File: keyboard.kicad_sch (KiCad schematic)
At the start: 35 parts, among them J1 USB_C_Receptacle_USB2.0, J2 USB_C_Receptacle_USB2.0, SW1 SW_Push, SW10 SW_Push, SW11 SW_Push, SW12 SW_Push, SW2 SW_Push, SW3 SW_Push, SW4 SW_Push, SW5 SW_Push, SW6 SW_Push, SW7 SW_Push, SW8 SW_Push, SW9 SW_Push, U1 PCA9555PW, U2 PCA9555PW, U3 SeeeduinoXIAO

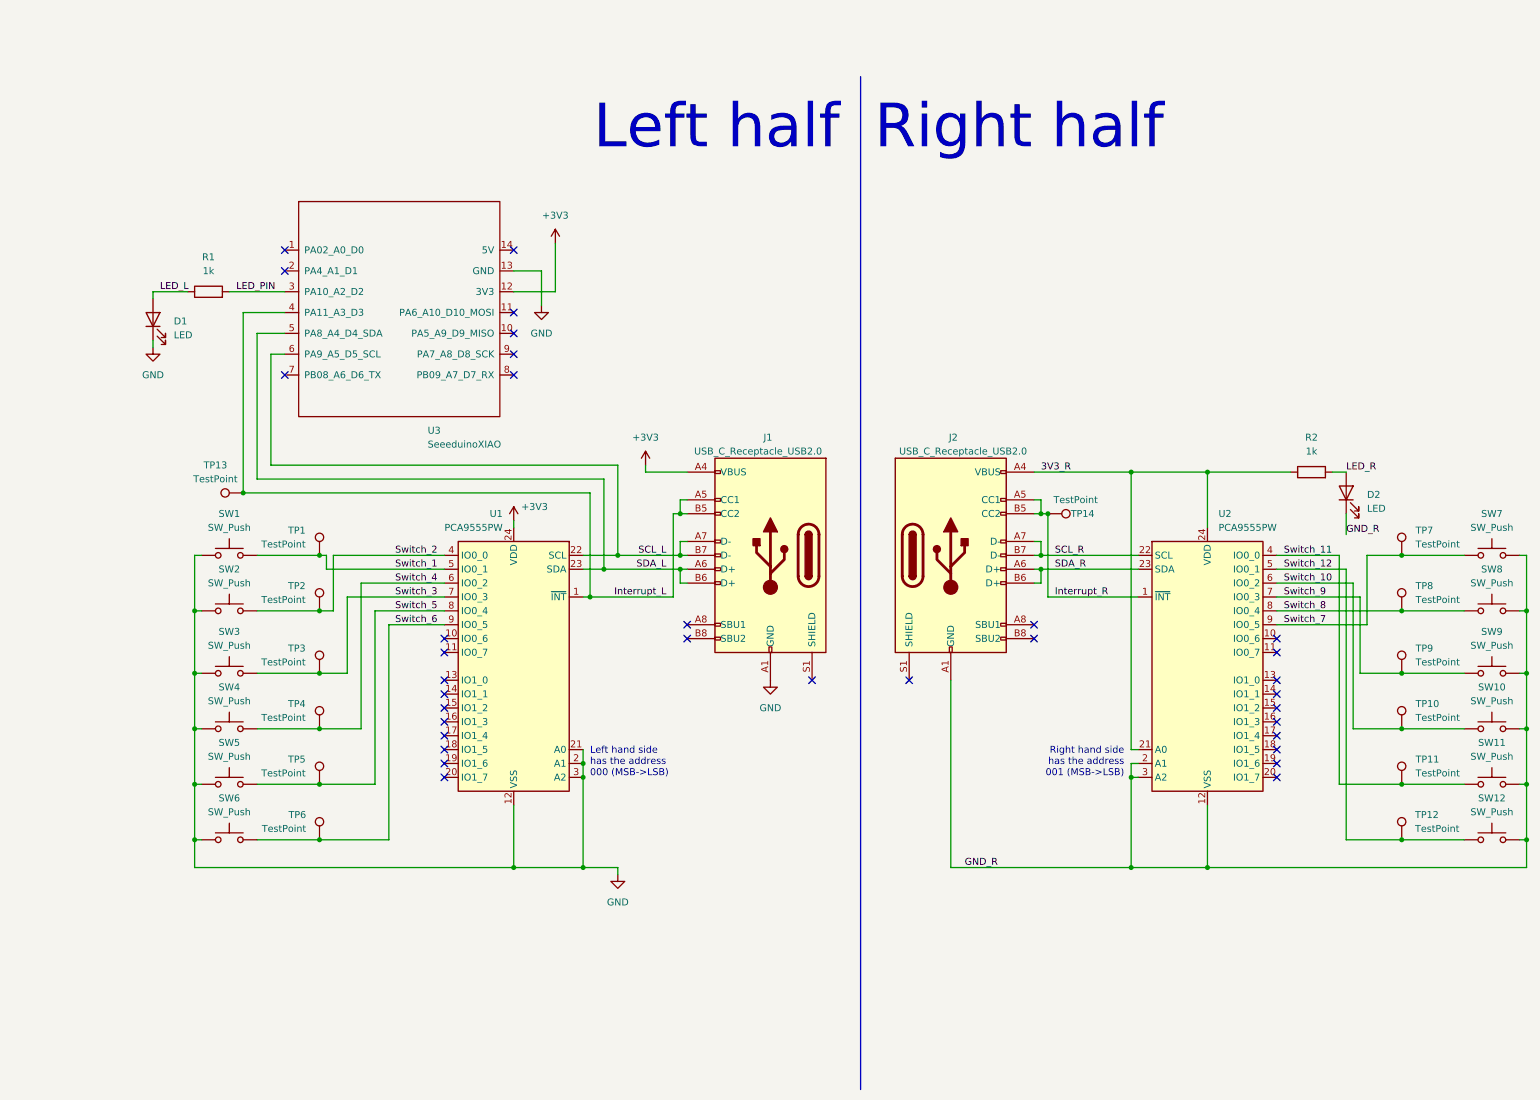
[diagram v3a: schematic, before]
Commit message: Went back to TRRS connection
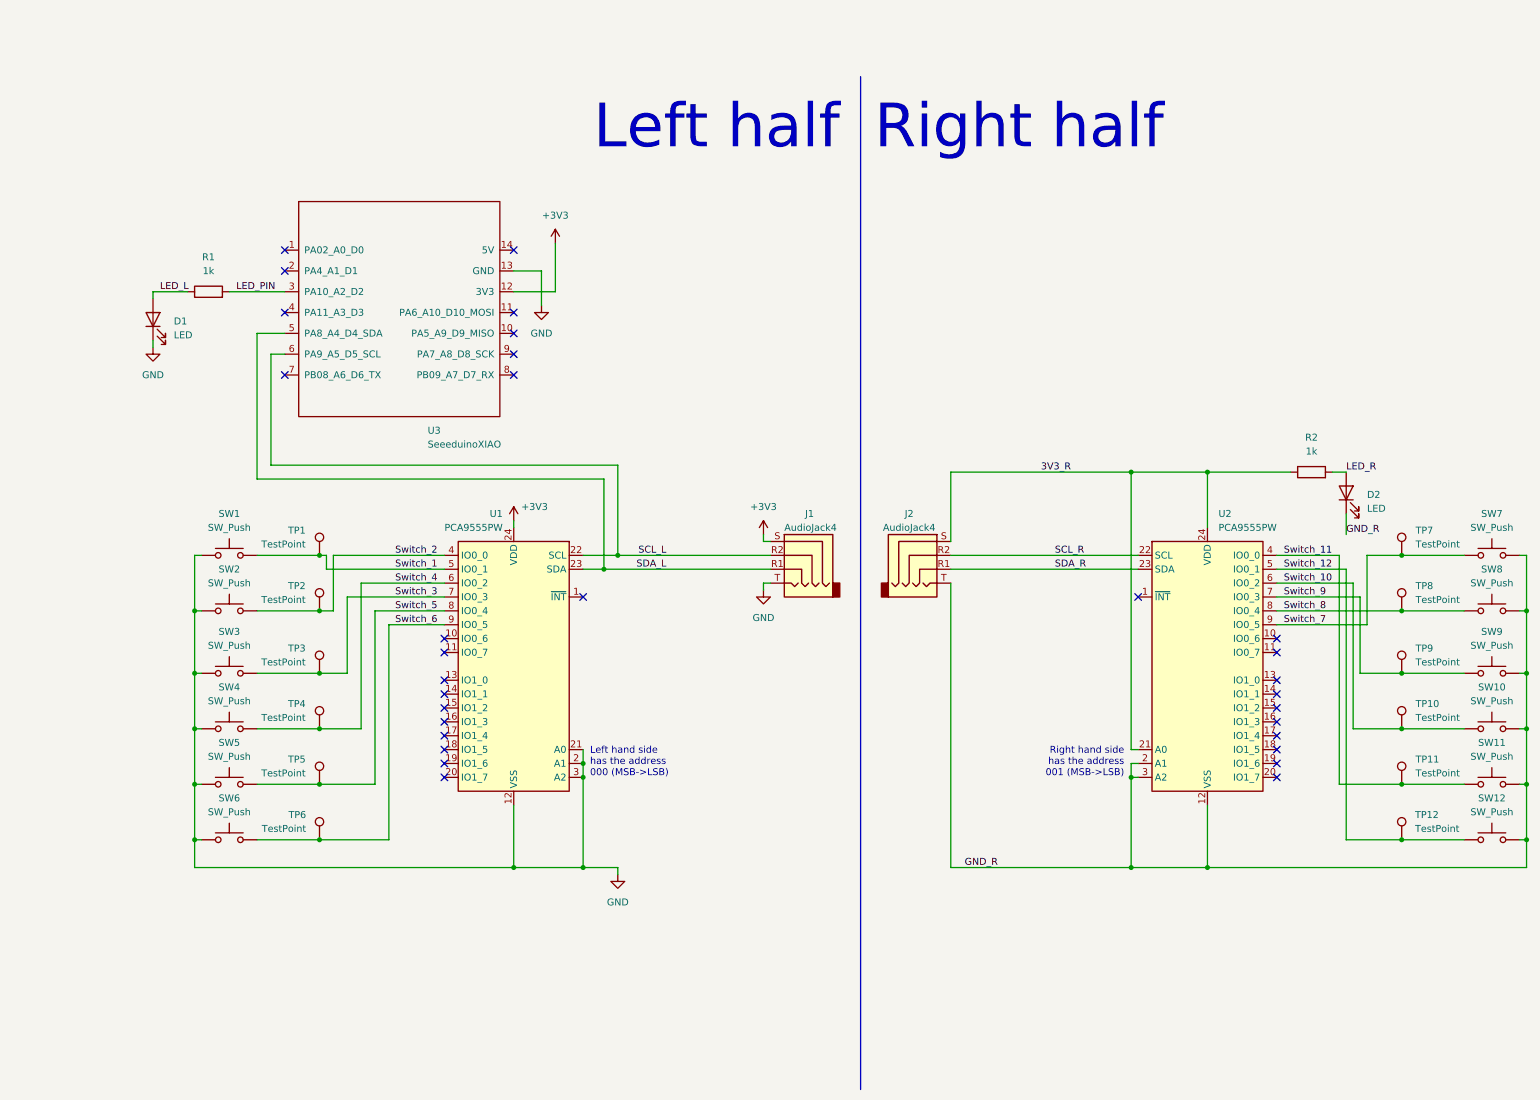
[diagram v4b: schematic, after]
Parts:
- removed J1, J2: USB_C_Receptacle_USB2.0, Connector_USB:USB_C_Receptacle_GCT_USB4105-xx-A_16P_TopMnt_Horizontal, symbol Connector:USB_C_Receptacle_USB2.0
- removed TP13, TP14: TestPoint, TestPoint:TestPoint_Pad_D1.0mm, symbol Connector:TestPoint
- added J1, J2: AudioJack4, Connector_Audio:Jack_3.5mm_PJ320D_Horizontal, symbol Connector:AudioJack4
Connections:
- net +3V3: now also J1.S
- net 3V3_R: now also J2.S
- net GND: now also J1.T
- net GND_R: now also J2.T
- net SCL_L: now also J1.R2
- net SCL_R: now also J2.R2
- net SDA_L: now also J1.R1
- net SDA_R: now also J2.R1
- net Interrupt_L: no longer names the net of U1.1 (~{INT})
- net Interrupt_L: no longer U3.4 (PA11_A3_D3)
- net Interrupt_R: no longer names the net of U2.1 (~{INT})
- no-connect marks 34 -> 31
